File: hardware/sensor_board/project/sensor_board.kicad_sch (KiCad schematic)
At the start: 18 parts, among them J1 Qwiic, J2 INT_HDR, U1 BMP581, U2 BMP581, U3 LSM6DSO32, U4 BNO085, U5 SHT40

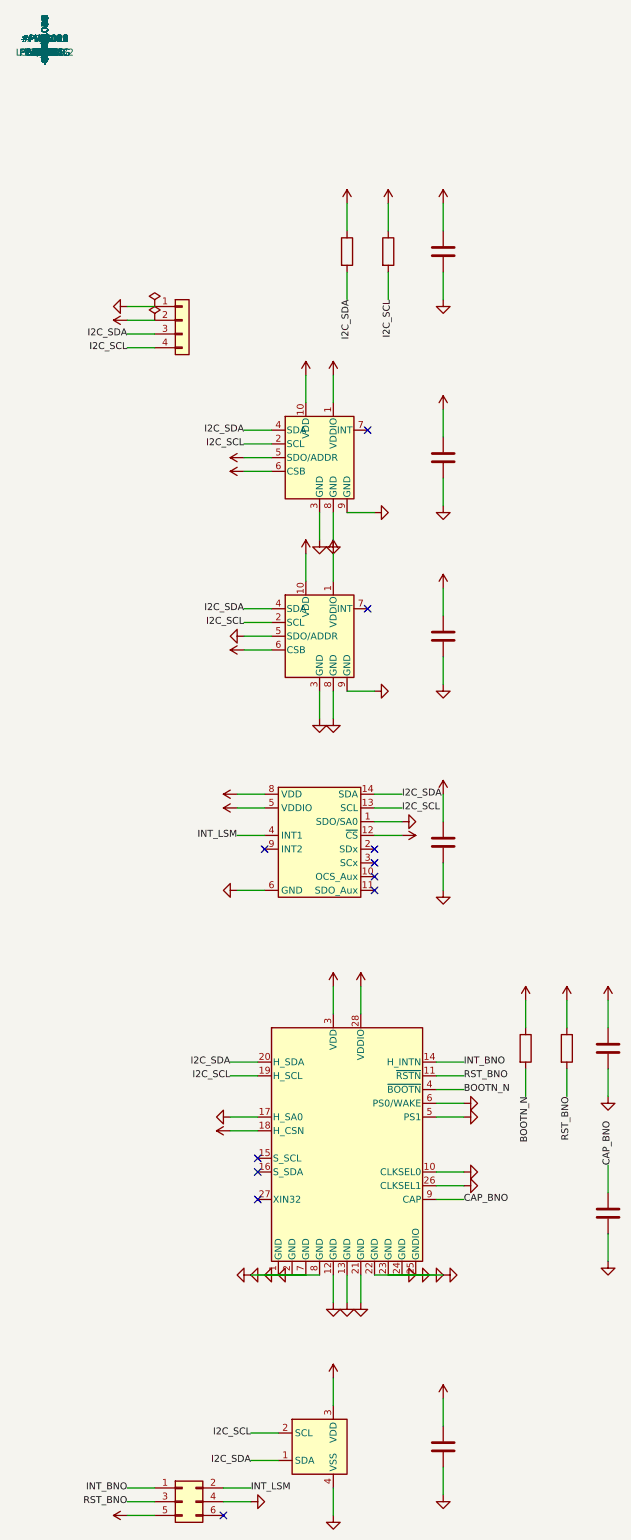
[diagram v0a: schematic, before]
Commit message: wip: Stand sichern - BNO085-Treiber, Sensor-Board-Iteration (DRC/Route), Terrain-Tools, Tests
- src/imu_bno085.h neu (SH-2 raw I2C), IMU-Abstraktion angepasst
- hardware/sensor_board: Generator + KiCad-Projekt aktualisiert, DRC-Reports
- tools/terrain: make_demo_pack.py, peaks_ch_raw.tsv, region_ch_v1.pack
- tests/ neu; platformio.ini, Screens, BLE/Fanet/Buzzer-Header

Co-Authored-By: Claude Fable 5 <noreply@anthropic.com>
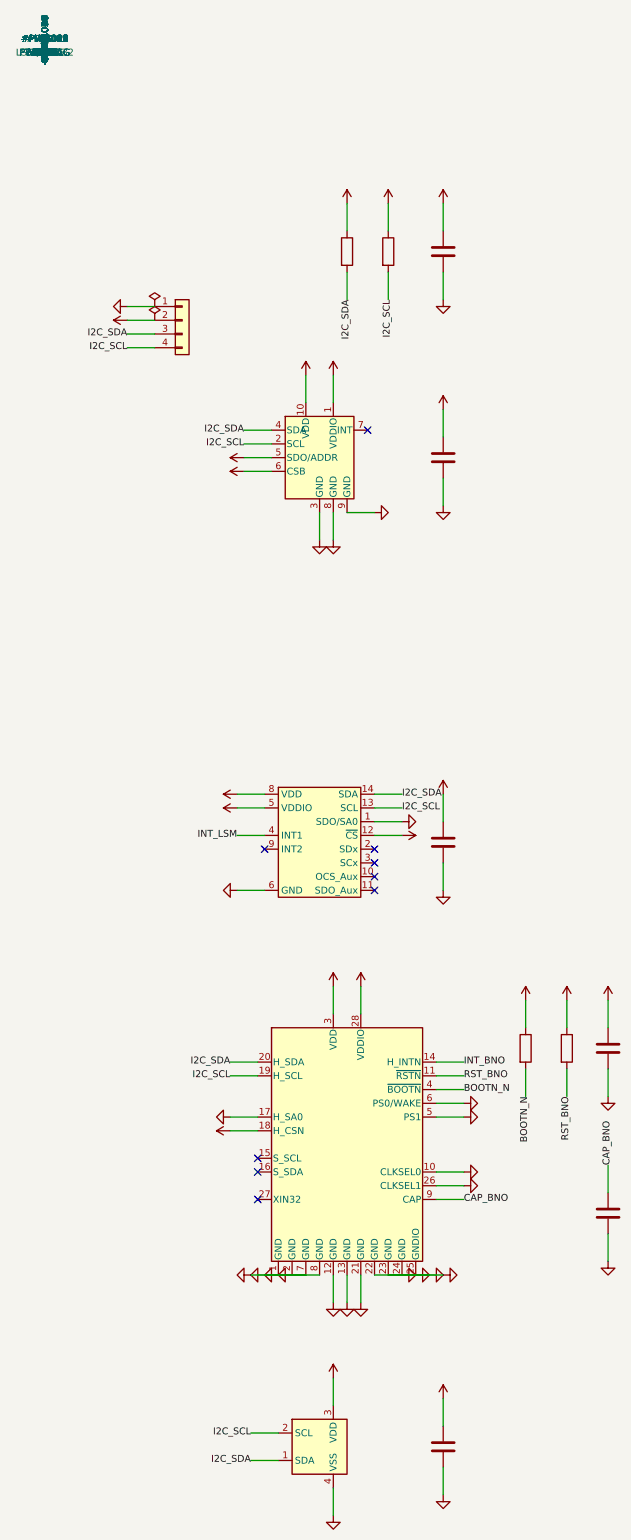
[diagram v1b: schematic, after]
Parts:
- removed C2: 100n, Capacitor_SMD:C_0402_1005Metric, symbol Device:C
- removed J2: INT_HDR, Connector_PinHeader_1.27mm:PinHeader_2x03_P1.27mm_Vertical, symbol Connector_Generic:Conn_02x03_Odd_Even
- removed U2: BMP581, aura_sensors:BMP581_LGA-10_2x2mm, symbol aura_sensors:BMP581
- U5: value SHT40 -> SHT45
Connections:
- no-connect marks 11 -> 9
